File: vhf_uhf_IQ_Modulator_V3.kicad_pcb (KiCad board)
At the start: 2 copper layers, 71 parts, among them J1 CONN_01X03, J2 TEST_1P, J3 Audio-Jack-3, J4 CONN_01X04, J5 SMA Edge FM, Q1 BC817-40, Q2 BC817-40, Q3 BC817-40, U1 TRF3701, U2 MMZ09332BT1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

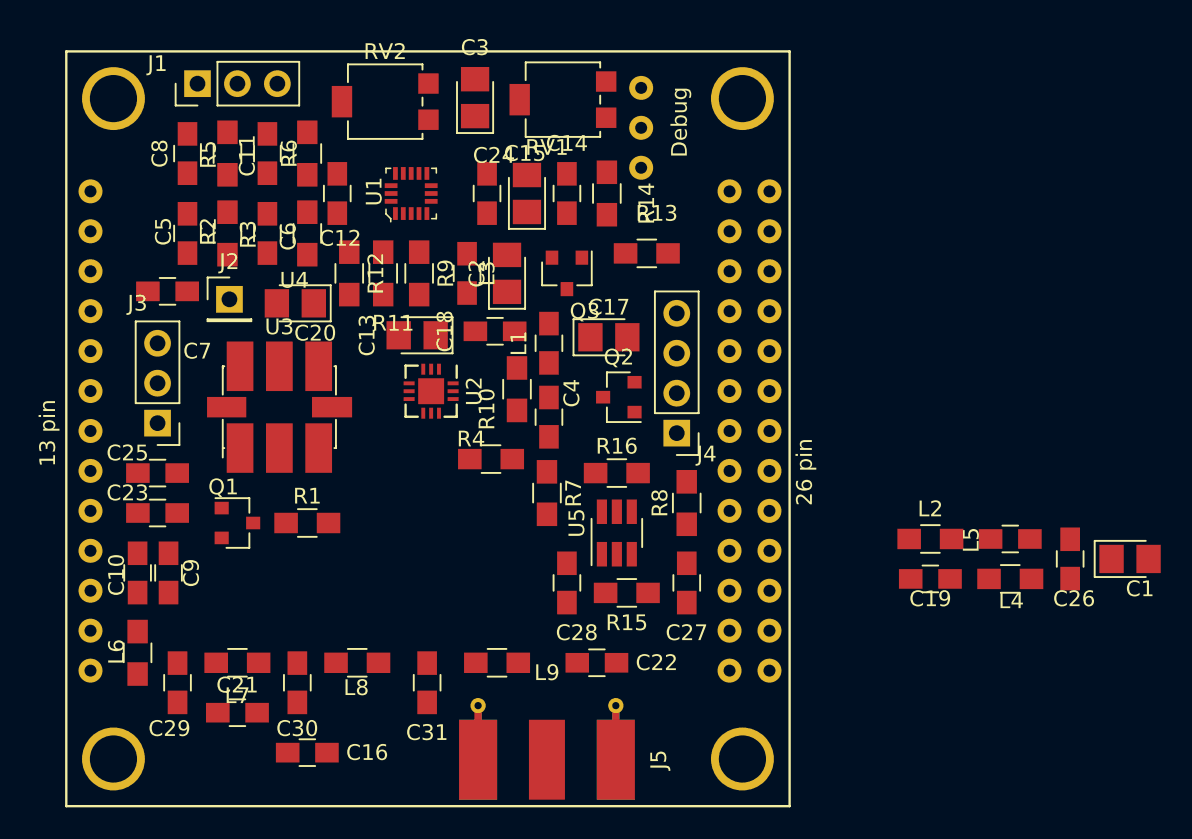
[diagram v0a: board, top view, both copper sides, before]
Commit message: fix lib and added Resistor
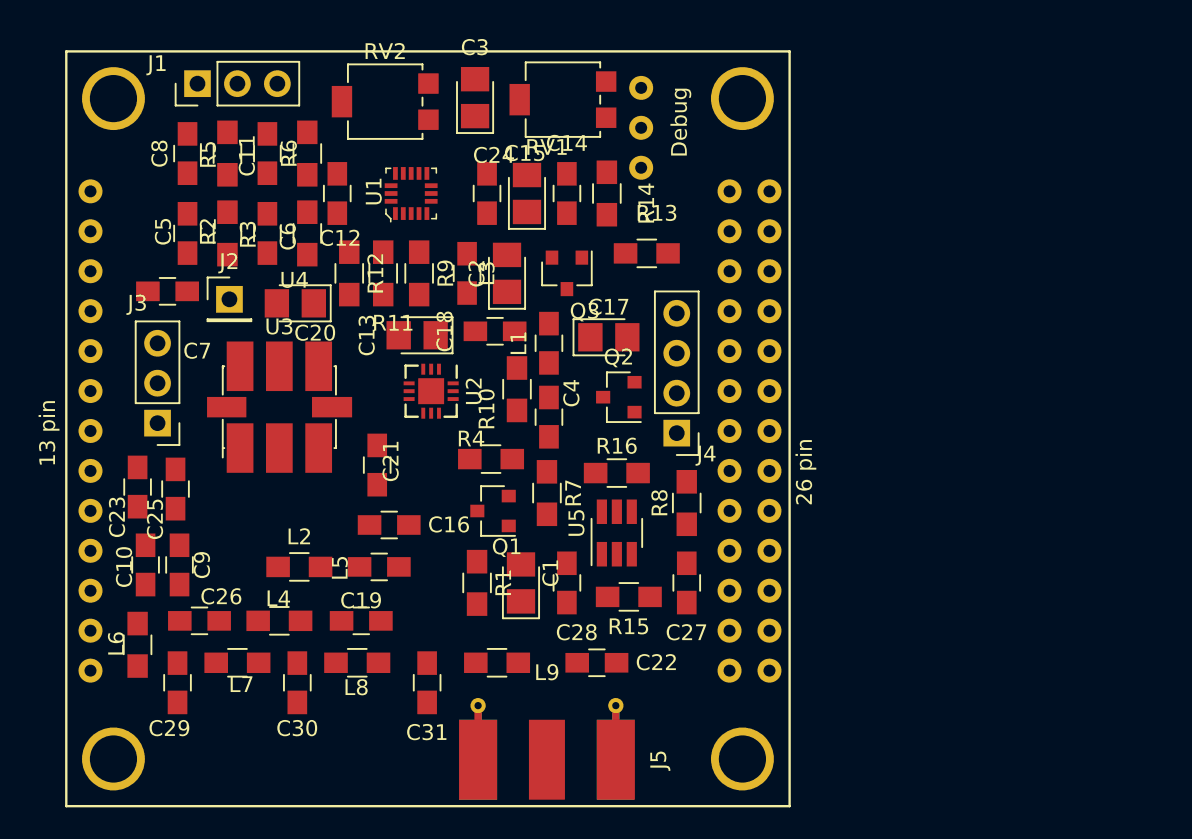
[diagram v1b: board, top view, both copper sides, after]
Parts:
- moved C26 55.5 mm to (157.0, 93.2), turned to 0 degrees
- moved L4 46.6 mm to (162.1, 93.2), turned to 180 degrees
- moved L2 40.2 mm to (163.3, 89.8)
- moved L5 40.2 mm to (168.4, 89.8)
- moved C1 38.8 mm to (177.4, 90.8), turned to 90 degrees
- moved C19 36.3 mm to (167.3, 93.2), turned to 0 degrees
- moved C21 18.1 mm to (168.3, 83.3), turned to 90 degrees
- moved Q1 16.3 mm to (175.6, 86.2), turned to 180 degrees
- moved C16 15.4 mm to (169.0, 87.1)
- moved R1 11.4 mm to (174.6, 90.8), turned to 270 degrees
- moved C23 2.08 mm to (153.0, 84.7), turned to 270 degrees
- moved C25 1.53 mm to (155.4, 84.8), turned to 270 degrees
- moved C9 0.86 mm to (155.7, 89.7)
- moved C10 0.72 mm to (153.5, 89.7)
- moved L6 0.51 mm to (153.0, 94.7)
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
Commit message: fix resistor
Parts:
- added R17: 4k7, Resistors_SMD:R_0805_HandSoldering, F.Cu at (184.3, 93.7)
- moved C22 22.5 mm to (160.5, 90.0), turned to 90 degrees
- moved C10 21.2 mm to (174.6, 87.2), turned to 0 degrees
- moved C9 19.4 mm to (174.6, 85.3), turned to 180 degrees
- moved L2 10.8 mm to (171.8, 83.1)
- moved R7 7.80 mm to (180.7, 77.5), turned to 90 degrees
- moved C19 6.76 mm to (170.4, 87.2), turned to 90 degrees
- moved L1 6.32 mm to (176.8, 81.4), turned to 180 degrees
- moved C18 5.34 mm to (170.4, 74.9), turned to 0 degrees
- moved L4 5.11 mm to (164.3, 88.6)
- moved C16 4.94 mm to (172.5, 90.7), turned to 270 degrees
- moved C13 4.70 mm to (175.5, 74.9)
- moved C26 4.70 mm to (157.0, 88.5)
- moved C4 3.89 mm to (176.8, 83.3), turned to 180 degrees
- moved R4 3.78 mm to (176.8, 79.4)
- moved L6 3.60 mm to (155.4, 92.1)
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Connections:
- Q1 pad 1: PA01 -> Net-(Q1-Pad1)
- U2 pad 4: (no net) -> Net-(U2-Pad4)

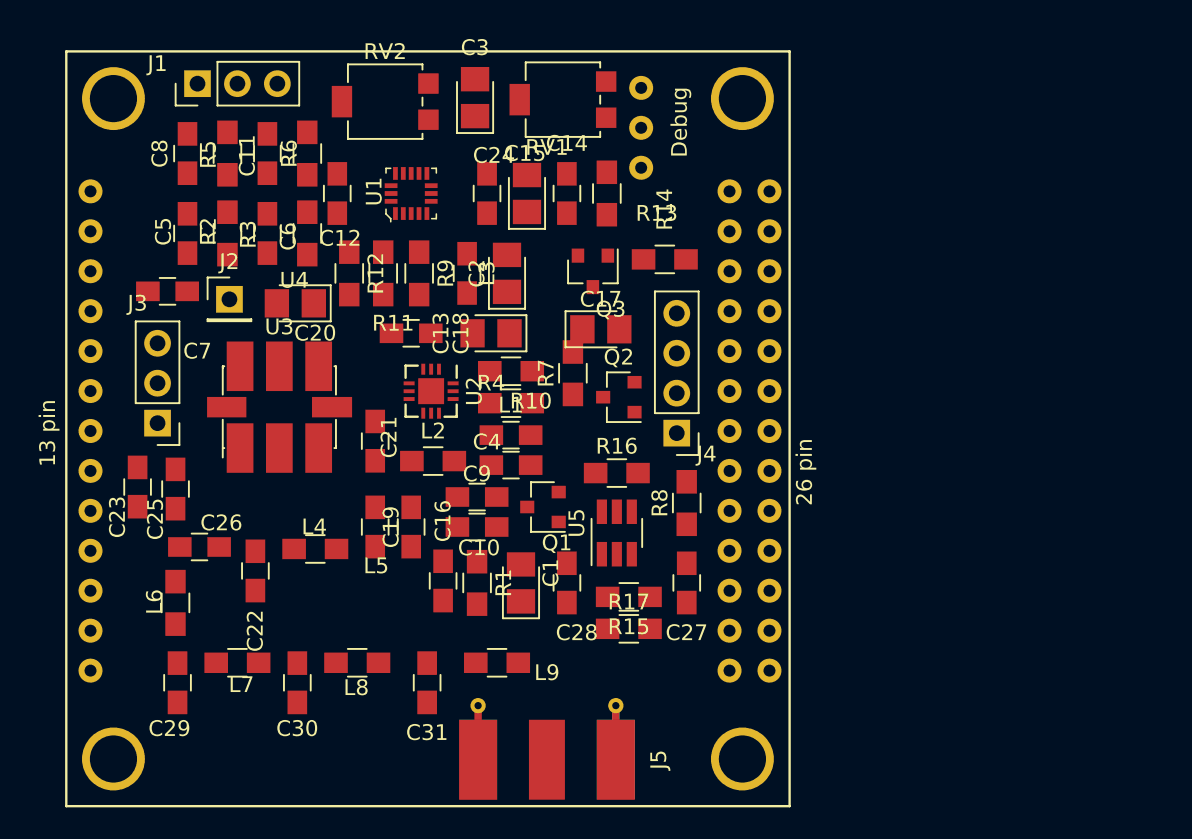
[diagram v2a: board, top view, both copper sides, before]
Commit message: ver3 Board plased
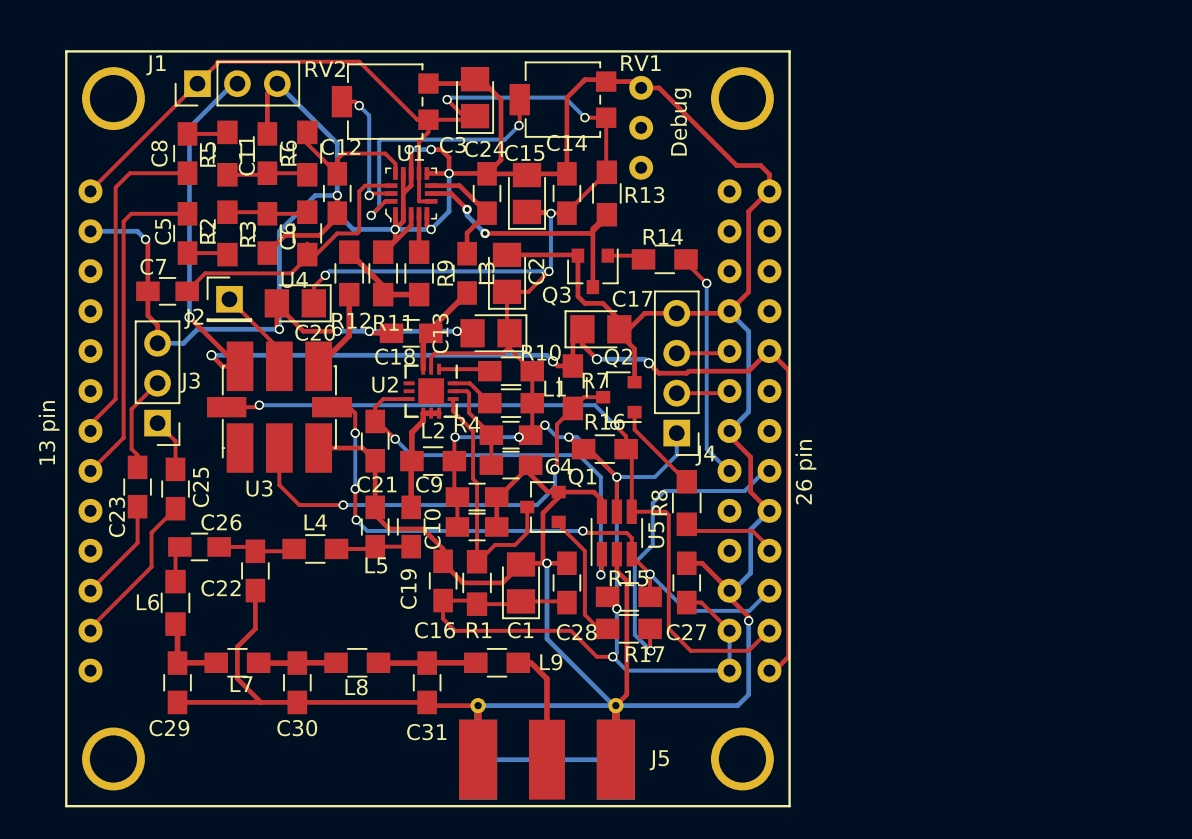
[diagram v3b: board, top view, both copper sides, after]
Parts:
- moved R16 1.70 mm to (182.8, 82.3)
- moved R7 0.89 mm to (180.7, 78.4)
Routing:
- net GND: track 0.00 -> 312.7 mm, vias 0 -> 13
- net +5V: track 0.00 -> 180.1 mm, vias 0 -> 12
- net +3V3: track 0.00 -> 84.5 mm, vias 0 -> 5
- net SDA: track 0.00 -> 48.4 mm, vias 0 -> 2
- net SLC: track 0.00 -> 39.8 mm, vias 0 -> 5
- net Net-(Q2-Pad3): track 0.00 -> 28.6 mm, vias 0 -> 2
- net PDet: track 0.00 -> 26.7 mm, vias 0 -> 2
- net Net-(C8-Pad1): track 0.00 -> 21.1 mm
- net Net-(C5-Pad1): track 0.00 -> 21.0 mm
- net PA01: track 0.00 -> 20.0 mm, vias 0 -> 1
- net Net-(C7-Pad1): track 0.00 -> 18.1 mm
- net Net-(Q3-Pad3): track 0.00 -> 18.0 mm, vias 0 -> 2
- net Net-(RV1-Pad2): track 0.00 -> 17.7 mm, vias 0 -> 2
- net Net-(Q1-Pad3): track 0.00 -> 16.6 mm
- net PA07: track 0.00 -> 14.6 mm, vias 0 -> 1
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
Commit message: ver3 Board plased
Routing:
- net GND: track 312.7 -> 316.2 mm
- net Net-(J5-Pad1): track 6.59 -> 7.54 mm
- net Net-(C19-Pad2): track 7.30 -> 7.80 mm
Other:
- board text added: "Giga Technology"
- board text added: "SDRTX_O_PI_1"
- board text added: "V1.0"
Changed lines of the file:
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@@
   (general
     (links 165)
-    (no_connects 5)
-    (area 148.0511 54.021666 194.787002 114.845001)
+    (no_connects 2)
+    (area 148.0511 48.98426 210.415 121.445001)
     (thickness 1.6)
-    (drawings 0)
-    (tracks 575)
+    (drawings 8)
+    (tracks 578)
     (zones 0)
     (modules 72)
@@
       (effects (font (size 1 1) (thickness 0.15)))
     )
-    (fp_text user "26 pin" (at 46.9519 -21.2471 270) (layer F.SilkS)
+    (fp_text user "26 pin" (at 43.2689 -41.1226) (layer F.SilkS)
       (effects (font (size 1 1) (thickness 0.15)))
     )
-    (fp_text user "13 pin" (at -1.1811 -23.7236 90) (layer F.SilkS)
+    (fp_text user "13 pin" (at 3.2639 -12.1666 90) (layer F.SilkS)
       (effects (font (size 1 1) (thickness 0.15)))
     )
@@
     )
   )
+  (dimension 40.005202 (width 0.3) (layer F.SilkS)
+    (gr_text "40.005 mm" (at 171.544006 50.397753 359.8181092) (layer F.SilkS)
+      (effects (font (size 1.5 1.5) (thickness 0.3)))
+    )
+    (feature1 (pts (xy 191.516 60.071) (xy 191.550792 49.11126)))
+    (feature2 (pts (xy 151.511 59.944) (xy 151.545792 48.98426)))
+    (crossbar (pts (xy 151.537221 51.684246) (xy 191.542221 51.811246)))
+    (arrow1a (pts (xy 191.542221 51.811246) (xy 190.413861 52.394088)))
+    (arrow1b (pts (xy 191.542221 51.811246) (xy 190.417585 51.221252)))
+    (arrow2a (pts (xy 151.537221 51.684246) (xy 152.661857 52.27424)))
+    (arrow2b (pts (xy 151.537221 51.684246) (xy 152.665581 51.101404)))
+  )
+  (dimension 41.91 (width 0.3) (layer F.SilkS)
+    (gr_text "41.910 mm" (at 203.915 81.026 270) (layer F.SilkS)
+      (effects (font (size 1.5 1.5) (thickness 0.3)))
+    )
+    (feature1 (pts (xy 191.516 101.981) (xy 205.265 101.981)))
+    (feature2 (pts (xy 191.516 60.071) (xy 205.265 60.071)))
+    (crossbar (pts (xy 202.565 60.071) (xy 202.565 101.981)))
+    (arrow1a (pts (xy 202.565 101.981) (xy 201.978579 100.854496)))
+    (arrow1b (pts (xy 202.565 101.981) (xy 203.151421 100.854496)))
+    (arrow2a (pts (xy 202.565 60.071) (xy 201.978579 61.197504)))
+    (arrow2b (pts (xy 202.565 60.071) (xy 203.151421 61.197504)))
+  )
+  (dimension 15.494 (width 0.3) (layer F.SilkS)
+    (gr_text "15.494 mm" (at 186.817 120.095) (layer F.SilkS)
+      (effects (font (size 1.5 1.5) (thickness 0.3)))
+    )
+    (feature1 (pts (xy 179.07 105.918) (xy 179.07 121.445)))
+    (feature2 (pts (xy 194.564 105.918) (xy 194.564 121.445)))
+    (crossbar (pts (xy 194.564 118.745) (xy 179.07 118.745)))
+    (arrow1a (pts (xy 179.07 118.745) (xy 180.196504 118.158579)))
+    (arrow1b (pts (xy 179.07 118.745) (xy 180.196504 119.331421)))
+    (arrow2a (pts (xy 194.564 118.745) (xy 193.437496 118.158579)))
+    (arrow2b (pts (xy 194.564 118.745) (xy 193.437496 119.331421)))
+  )
+  (dimension 48.006 (width 0.3) (layer F.SilkS)
+    (gr_text "48.006 mm" (at 199.724 81.026 270) (layer F.SilkS)
+      (effects (font (size 1.5 1.5) (thickness 0.3)))
+    )
+    (feature1 (pts (xy 195.199 105.029) (xy 201.074 105.029)))
+    (feature2 (pts (xy 195.199 57.023) (xy 201.074 57.023)))
+    (crossbar (pts (xy 198.374 57.023) (xy 198.374 105.029)))
+    (arrow1a (pts (xy 198.374 105.029) (xy 197.787579 103.902496)))
+    (arrow1b (pts (xy 198.374 105.029) (xy 198.960421 103.902496)))
+    (arrow2a (pts (xy 198.374 57.023) (xy 197.787579 58.149504)))
+    (arrow2b (pts (xy 198.374 57.023) (xy 198.960421 58.149504)))
+  )
+  (dimension 46.101 (width 0.3) (layer F.SilkS)
+    (gr_text "46.101 mm" (at 171.5135 53.641) (layer F.SilkS)
+      (effects (font (size 1.5 1.5) (thickness 0.3)))
+    )
+    (feature1 (pts (xy 194.564 56.515) (xy 194.564 52.291)))
+    (feature2 (pts (xy 148.463 56.515) (xy 148.463 52.291)))
+    (crossbar (pts (xy 148.463 54.991) (xy 194.564 54.991)))
+    (arrow1a (pts (xy 194.564 54.991) (xy 193.437496 55.577421)))
+    (arrow1b (pts (xy 194.564 54.991) (xy 193.437496 54.404579)))
+    (arrow2a (pts (xy 148.463 54.991) (xy 149.589504 55.577421)))
+    (arrow2b (pts (xy 148.463 54.991) (xy 149.589504 54.404579)))
+  )
+  (gr_text SDRTX_O_PI_1 (at 162.814 93.345) (layer F.SilkS)
+    (effects (font (size 1.1 1.1) (thickness 0.275)))
+  )
+  (gr_text V1.0 (at 151.511 98.679) (layer F.SilkS)
+    (effects (font (size 1.5 1.5) (thickness 0.3)))
+  )
+  (gr_text "Giga Technology" (at 163.195 103.378) (layer F.Cu)
+    (effects (font (size 1.4 1.4) (thickness 0.3)))
+  )
   (via (at 180.467 81.534) (size 0.6) (drill 0.4) (layers F.Cu B.Cu) (net 1))
   (segment (start 180.467 81.534) (end 181.229 82.296) (width 0.25) (layer F.Cu) (net 1))
@@
   (segment (start 182.836 61.221) (end 182.836 64.646) (width 0.25) (layer F.Cu) (net 1))
   (segment (start 182.836 64.646) (end 182.88 64.69) (width 0.25) (layer F.Cu) (net 1))
+  (segment (start 183.45 102.05) (end 183.45 98.61) (width 0.3) (layer B.Cu) (net 2) (status C00000))
   (segment (start 174.69 102.05) (end 183.45 102.05) (width 0.3) (layer B.Cu) (net 2))
   (segment (start 170.434 64.765) (end 170.434 65.532) (width 0.3) (layer F.Cu) (net 2))
@@
   (segment (start 190.6811 91.3036) (end 190.6811 91.7481) (width 0.3) (layer F.Cu) (net 2))
   (segment (start 190.6811 91.7481) (end 191.897 92.964) (width 0.3) (layer F.Cu) (net 2))
-  (segment (start 191.204 98.61) (end 183.45 98.61) (width 0.3) (layer B.Cu) (net 2))
-  (segment (start 191.897 97.917) (end 191.204 98.61) (width 0.3) (layer B.Cu) (net 2))
-  (segment (start 191.897 93.218) (end 191.897 97.917) (width 0.3) (layer B.Cu) (net 2))
-  (via (at 191.897 93.218) (size 0.6) (drill 0.4) (layers F.Cu B.Cu) (net 2))
   (segment (start 191.897 92.964) (end 191.897 93.218) (width 0.3) (layer F.Cu) (net 2))
+  (via (at 191.897 93.218) (size 0.6) (drill 0.4) (layers F.Cu B.Cu) (net 2))
+  (segment (start 191.897 93.218) (end 191.897 97.917) (width 0.3) (layer B.Cu) (net 2))
+  (segment (start 191.897 97.917) (end 191.204 98.61) (width 0.3) (layer B.Cu) (net 2))
+  (segment (start 191.204 98.61) (end 183.45 98.61) (width 0.3) (layer B.Cu) (net 2))
   (segment (start 179.816 85.029) (end 179.816 85.36) (width 0.3) (layer F.Cu) (net 2))
   (segment (start 179.816 85.36) (end 178.816 86.36) (width 0.3) (layer F.Cu) (net 2))
@@
   (segment (start 168.148 86.487) (end 168.148 85.999) (width 0.3) (layer F.Cu) (net 2))
   (segment (start 183.515 88.98) (end 183.515 90.043) (width 0.3) (layer F.Cu) (net 2))
-  (segment (start 183.515 90.043) (end 184.15 90.678) (width 0.3) (layer F.Cu) (net 2))
-  (segment (start 184.15 90.678) (end 184.15 97.91) (width 0.3) (layer F.Cu) (net 2))
   (segment (start 184.15 97.91) (end 183.45 98.61) (width 0.3) (layer F.Cu) (net 2))
+  (segment (start 184.15 90.678) (end 184.15 97.91) (width 0.3) (layer F.Cu) (net 2))
+  (segment (start 183.515 90.043) (end 184.15 90.678) (width 0.3) (layer F.Cu) (net 2))
   (segment (start 187.325 73.66) (end 190.5447 73.66) (width 0.3) (layer F.Cu) (net 2))
   (segment (start 190.5447 73.66) (end 190.6811 73.5236) (width 0.3) (layer F.Cu) (net 2))
@@
   (segment (start 165.688 88.646) (end 168.001 88.646) (width 0.25) (layer F.Cu) (net 14))
   (segment (start 168.001 88.646) (end 168.148 88.499) (width 0.25) (layer F.Cu) (net 14))
+  (segment (start 171.704 80.013) (end 172.204 80.013) (width 0.36) (layer F.Cu) (net 15) (status C00000))
   (segment (start 172.204 80.013) (end 171.204 80.013) (width 0.36) (layer F.Cu) (net 15))
   (segment (start 171.204 80.013) (end 171.204 80.51) (width 0.36) (layer F.Cu) (net 15))
@@
   (segment (start 187.325 76.2) (end 190.5447 76.2) (width 0.25) (layer F.Cu) (net 29))
   (segment (start 190.5447 76.2) (end 190.6811 76.0636) (width 0.25) (layer F.Cu) (net 29))
-  (segment (start 179.07 102.05) (end 179.07 96.901) (width 0.36) (layer F.Cu) (net 30))
-  (segment (start 179.07 96.901) (end 178.054 95.885) (width 0.36) (layer F.Cu) (net 30))
+  (segment (start 177.245 95.885) (end 178.308 95.885) (width 0.36) (layer F.Cu) (net 30) (status 400000))
+  (segment (start 179.07 96.647) (end 179.07 102.05) (width 0.36) (layer F.Cu) (net 30) (status 800000))
+  (segment (start 178.308 95.885) (end 179.07 96.647) (width 0.36) (layer F.Cu) (net 30))
   (segment (start 193.2211 83.6836) (end 192.9224 83.6836) (width 0.25) (layer B.Cu) (net 31))
   (segment (start 192.9224 83.6836) (end 191.643 84.963) (width 0.25) (layer B.Cu) (net 31))

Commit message: Board now compleat with Groundplane
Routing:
- added copper zone on B.Cu, net GND
- added copper zone on F.Cu, net GND
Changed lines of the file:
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@@
   (general
     (links 165)
-    (no_connects 2)
+    (no_connects 0)
     (area 148.0511 48.98426 210.415 121.445001)
     (thickness 1.6)
@@
   (segment (start 182.836 61.221) (end 182.836 64.646) (width 0.25) (layer F.Cu) (net 1))
   (segment (start 182.836 64.646) (end 182.88 64.69) (width 0.25) (layer F.Cu) (net 1))
-  (segment (start 183.45 102.05) (end 183.45 98.61) (width 0.3) (layer B.Cu) (net 2) (status C00000))
+  (segment (start 183.45 102.05) (end 183.45 98.61) (width 0.3) (layer B.Cu) (net 2))
   (segment (start 174.69 102.05) (end 183.45 102.05) (width 0.3) (layer B.Cu) (net 2))
   (segment (start 170.434 64.765) (end 170.434 65.532) (width 0.3) (layer F.Cu) (net 2))
@@
   (segment (start 165.688 88.646) (end 168.001 88.646) (width 0.25) (layer F.Cu) (net 14))
   (segment (start 168.001 88.646) (end 168.148 88.499) (width 0.25) (layer F.Cu) (net 14))
-  (segment (start 171.704 80.013) (end 172.204 80.013) (width 0.36) (layer F.Cu) (net 15) (status C00000))
+  (segment (start 171.704 80.013) (end 172.204 80.013) (width 0.36) (layer F.Cu) (net 15))
   (segment (start 172.204 80.013) (end 171.204 80.013) (width 0.36) (layer F.Cu) (net 15))
   (segment (start 171.204 80.013) (end 171.204 80.51) (width 0.36) (layer F.Cu) (net 15))
@@
   (segment (start 187.325 76.2) (end 190.5447 76.2) (width 0.25) (layer F.Cu) (net 29))
   (segment (start 190.5447 76.2) (end 190.6811 76.0636) (width 0.25) (layer F.Cu) (net 29))
-  (segment (start 177.245 95.885) (end 178.308 95.885) (width 0.36) (layer F.Cu) (net 30) (status 400000))
-  (segment (start 179.07 96.647) (end 179.07 102.05) (width 0.36) (layer F.Cu) (net 30) (status 800000))
+  (segment (start 177.245 95.885) (end 178.308 95.885) (width 0.36) (layer F.Cu) (net 30))
+  (segment (start 179.07 96.647) (end 179.07 102.05) (width 0.36) (layer F.Cu) (net 30))
   (segment (start 178.308 95.885) (end 179.07 96.647) (width 0.36) (layer F.Cu) (net 30))
   (segment (start 193.2211 83.6836) (end 192.9224 83.6836) (width 0.25) (layer B.Cu) (net 31))
@@
   (segment (start 181.483 88.773) (end 179.816 87.106) (width 0.25) (layer F.Cu) (net 69))
   (segment (start 179.816 87.106) (end 179.816 86.929) (width 0.25) (layer F.Cu) (net 69))
+  (zone (net 2) (net_name GND) (layer F.Cu) (hatch edge 0.508)
+    (connect_pads (clearance 0.508))
+    (min_thickness 0.254)
+    (fill yes (arc_segments 16) (thermal_gap 0.508) (thermal_bridge_width 0.508))
+    (polygon
+      (pts
+        (xy 148.463 57.023) (xy 148.336 105.029) (xy 194.437 105.029) (xy 194.437 57.023) (xy 148.463 56.896)
+      )
+    )
+  )
+  (zone (net 2) (net_name GND) (layer B.Cu) (hatch edge 0.508)
+    (connect_pads (clearance 0.508))
+    (min_thickness 0.254)
+    (fill yes (arc_segments 16) (thermal_gap 0.508) (thermal_bridge_width 0.508))
+    (polygon
+      (pts
+        (xy 148.463 57.023) (xy 148.336 105.029) (xy 194.437 105.029) (xy 194.437 57.023) (xy 148.463 56.896)
+      )
+    )
+  )
 )
